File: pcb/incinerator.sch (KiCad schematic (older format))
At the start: 39 parts, among them J1 IGNITION1, J2 IGNITION2, J3 VALVE1, J4 VALVE2, J5 VALVE3, J6 AIRPMP, J7 Power Source 12V, J8 Waveshare 4.2\" e-paper, Q1 IRLU120N, Q2 IRLU120N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

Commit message: Added ctrl leds to furnace terminals
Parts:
- removed C1: 10u, symbol Device:C
- removed D2, D4, D6: D, symbol Device:D
- removed J5: VALVE3, symbol Connector:Screw_Terminal_01x02
- removed R2, R3: 15k, symbol Device:R
- added C1: 4.7u, symbol Device:CP
- added D10, D6, D8: GRN, symbol Device:LED
- added D11, D7, D9: D, symbol Device:D
- added D12: YLW, symbol Device:LED
- added D2, D4: RED, symbol Device:LED
- added J7: AIRPMP, symbol Connector:Screw_Terminal_01x02
- added R1, R13, R16, R7: 47, symbol Device:R
- added R14, R17: 100, symbol Device:R
- added R15, R18: 15k, symbol Device:R
- J1: value IGNITION1 -> IGNITION_MAIN
- J2: value IGNITION2 -> IGNITION_AFT
- J3: value VALVE1 -> VALVE_MAIN
- J4: value VALVE2 -> VALVE_AFT_HI
- J6: value AIRPMP -> VALVE_AFT_LO
- R10: value 100 -> 47
- R12, R9: value 100 -> 15k
- R4: value 15k -> 47
- R5: value 15k -> 100
- gave numbers to parts that had none: 2
- renumbered J8 to J5, J7 to J8, R7 to R2, R1 to R3, U2 to U1, U1 to U4
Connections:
- wire segments 175 -> 181
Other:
- moved on the sheet: D1, J1, Q1, R2, R3

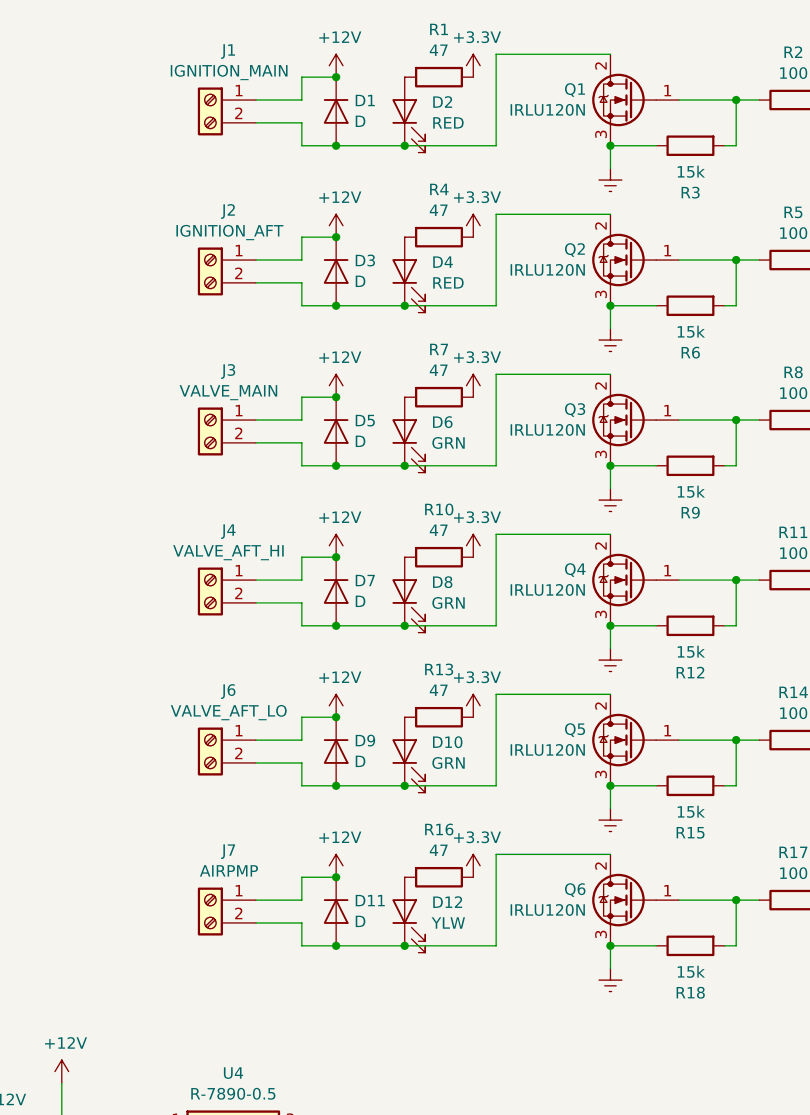
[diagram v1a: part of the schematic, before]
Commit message: reassigned symbols
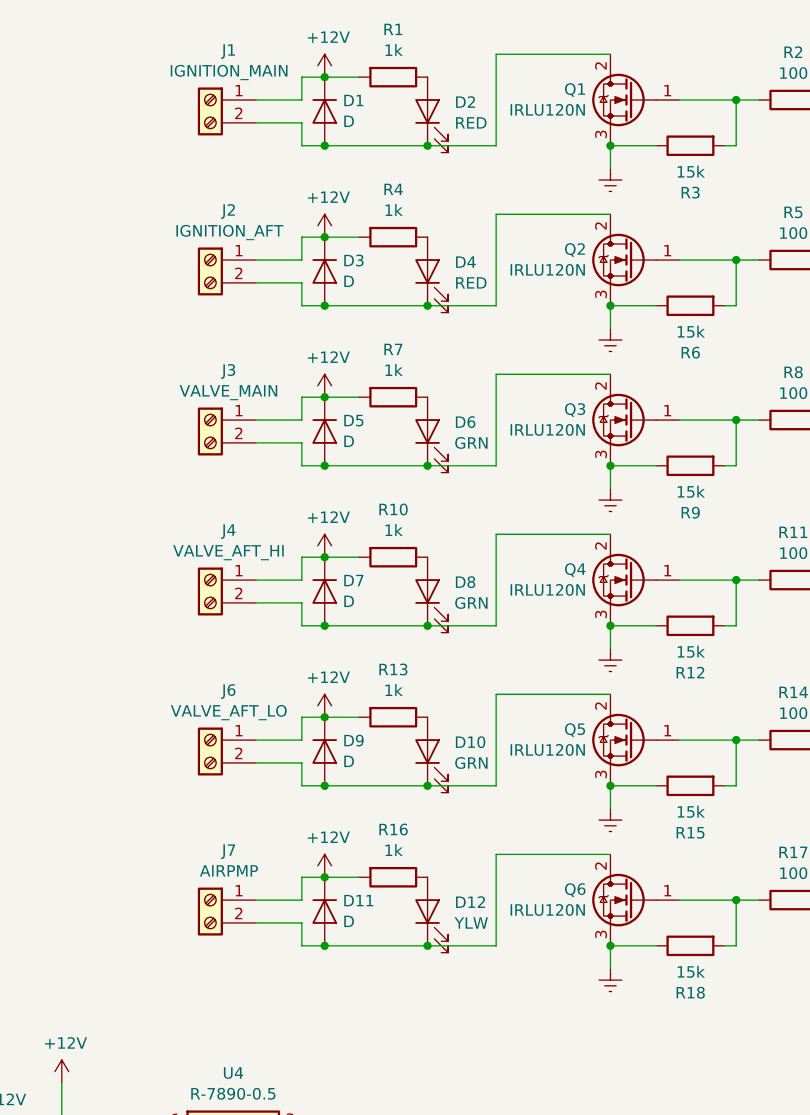
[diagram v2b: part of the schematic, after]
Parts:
- R1, R10, R13, R16, R4, R7: value 47 -> 1k
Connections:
- net +12V: now also R1.2, R10.2, R13.2, R16.2, R4.2, R7.2
- net +3V3: no longer R1.1, R10.1, R13.1, R16.1, R4.1, R7.1
- net at D2.2 (A): now also R1.1; no longer R1.2
- net at D4.2 (A): now also R4.1; no longer R4.2
- net at D6.2 (A): now also R7.1; no longer R7.2
- net at D8.2 (A): now also R10.1; no longer R10.2
- net at D10.2 (A): now also R13.1; no longer R13.2
- net at D12.2 (A): now also R16.1; no longer R16.2
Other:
- moved on the sheet: D1, D10, D11, D12, D2, D3, D4, D5, D6, D7, D8, D9

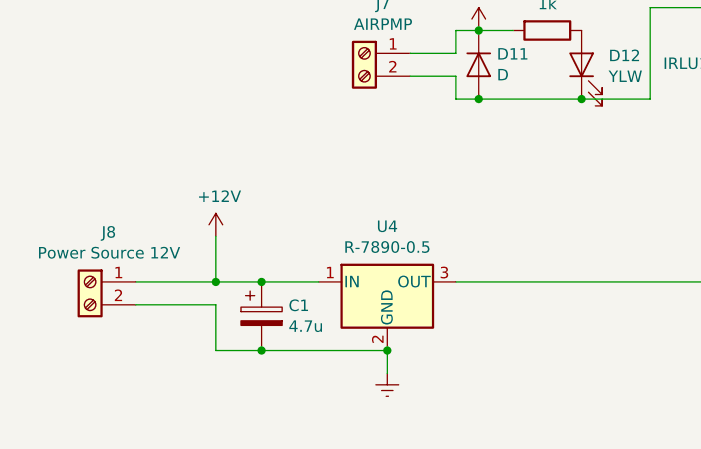
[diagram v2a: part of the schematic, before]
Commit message: Add power flags to satisfy KiCad electrical rule check
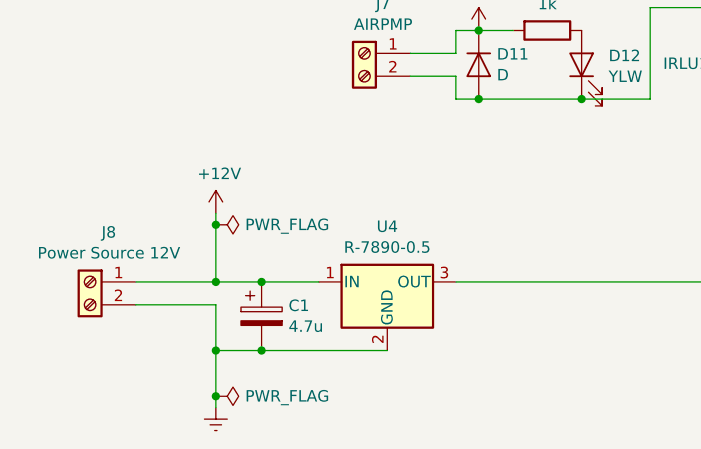
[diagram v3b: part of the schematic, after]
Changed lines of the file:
@@
 L power:Earth #PWR025
 U 1 1 5E159756
-P 2450 6450
-F 0 "#PWR025" H 2450 6200 50  0001 C CNN
-F 1 "Earth" H 2450 6300 50  0001 C CNN
-F 2 "" H 2450 6450 50  0001 C CNN
-F 3 "~" H 2450 6450 50  0001 C CNN
-	1    2450 6450
+P 1700 6600
+F 0 "#PWR025" H 1700 6350 50  0001 C CNN
+F 1 "Earth" H 1700 6450 50  0001 C CNN
+F 2 "" H 1700 6600 50  0001 C CNN
+F 3 "~" H 1700 6600 50  0001 C CNN
+	1    1700 6600
 	1    0    0    -1
 $EndComp
 Wire Wire Line
 	1350 6150 1700 6150
-$Comp
-L power:+12V #PWR022
-U 1 1 5E1590DD
-P 1700 5850
-F 0 "#PWR022" H 1700 5700 50  0001 C CNN
-F 1 "+12V" H 1715 6023 50  0000 C CNN
-F 2 "" H 1700 5850 50  0001 C CNN
-F 3 "" H 1700 5850 50  0001 C CNN
-	1    1700 5850
-	1    0    0    -1
-$EndComp
 Wire Wire Line
 	5450 3950 5450 3650
@@
 Wire Wire Line
 	1350 6050 1700 6050
-Wire Wire Line
-	1700 6050 1700 5850
 Connection ~ 1700 6050
 Wire Wire Line
 	1700 6150 1700 6350
-Wire Wire Line
-	2450 6450 2450 6350
-Connection ~ 2450 6350
 Wire Wire Line
 	2750 6050 5750 6050
@@
 Wire Wire Line
 	2850 4950 3000 4950
+Wire Wire Line
+	1700 6600 1700 6550
+Connection ~ 1700 6350
+$Comp
+L power:PWR_FLAG #FLG0101
+U 1 1 5E1C89C2
+P 1700 6550
+F 0 "#FLG0101" H 1700 6625 50  0001 C CNN
+F 1 "PWR_FLAG" V 1700 6678 50  0000 L CNN
+F 2 "" H 1700 6550 50  0001 C CNN
+F 3 "~" H 1700 6550 50  0001 C CNN
+	1    1700 6550
+	0    1    1    0
+$EndComp
+Connection ~ 1700 5800
+Wire Wire Line
+	1700 5800 1700 5750
+Connection ~ 1700 6550
+Wire Wire Line
+	1700 6550 1700 6350
+Wire Wire Line
+	1700 6050 1700 5800
+$Comp
+L power:PWR_FLAG #FLG0102
+U 1 1 5E1C8CFC
+P 1700 5800
+F 0 "#FLG0102" H 1700 5875 50  0001 C CNN
+F 1 "PWR_FLAG" V 1700 5928 50  0000 L CNN
+F 2 "" H 1700 5800 50  0001 C CNN
+F 3 "~" H 1700 5800 50  0001 C CNN
+	1    1700 5800
+	0    1    1    0
+$EndComp
+$Comp
+L power:+12V #PWR022
+U 1 1 5E1590DD
+P 1700 5750
+F 0 "#PWR022" H 1700 5600 50  0001 C CNN
+F 1 "+12V" H 1715 5923 50  0000 C CNN
+F 2 "" H 1700 5750 50  0001 C CNN
+F 3 "" H 1700 5750 50  0001 C CNN
+	1    1700 5750
+	1    0    0    -1
+$EndComp
 $EndSCHEMATC
